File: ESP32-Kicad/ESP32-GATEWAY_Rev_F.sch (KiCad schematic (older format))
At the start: 65 parts, among them J1 Conn_01x07_Male, T1 DTC114YKA, U1 ACPL-217-56AE, U2 TLV62569DBVT(SOT23-5), U3 ESP32-WROOM-32D-4MB, U4 LAN8710A-EZC(QFN32), U5 ACPL-217-56AE

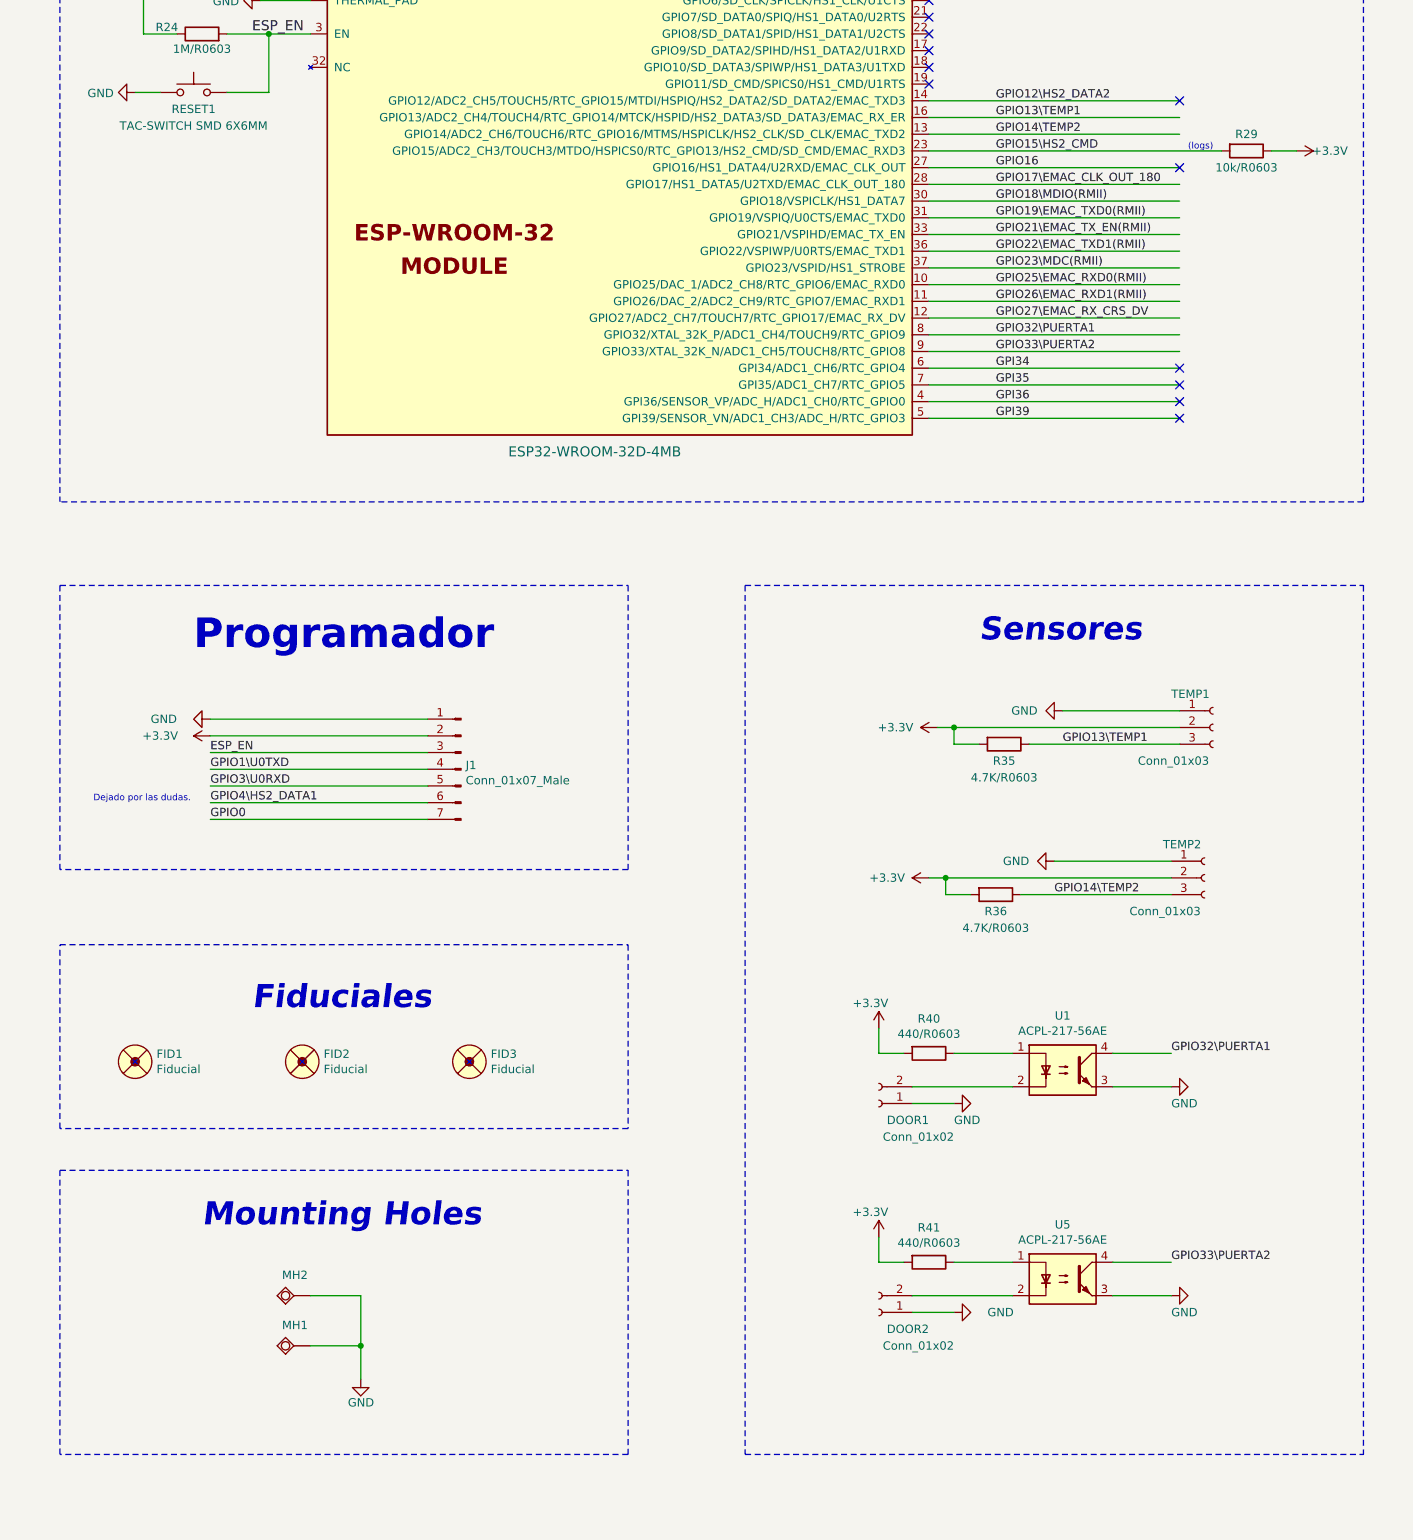
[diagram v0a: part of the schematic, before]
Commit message: Se agregaron 2 sensores de puerta y se sacó uno de temperatura
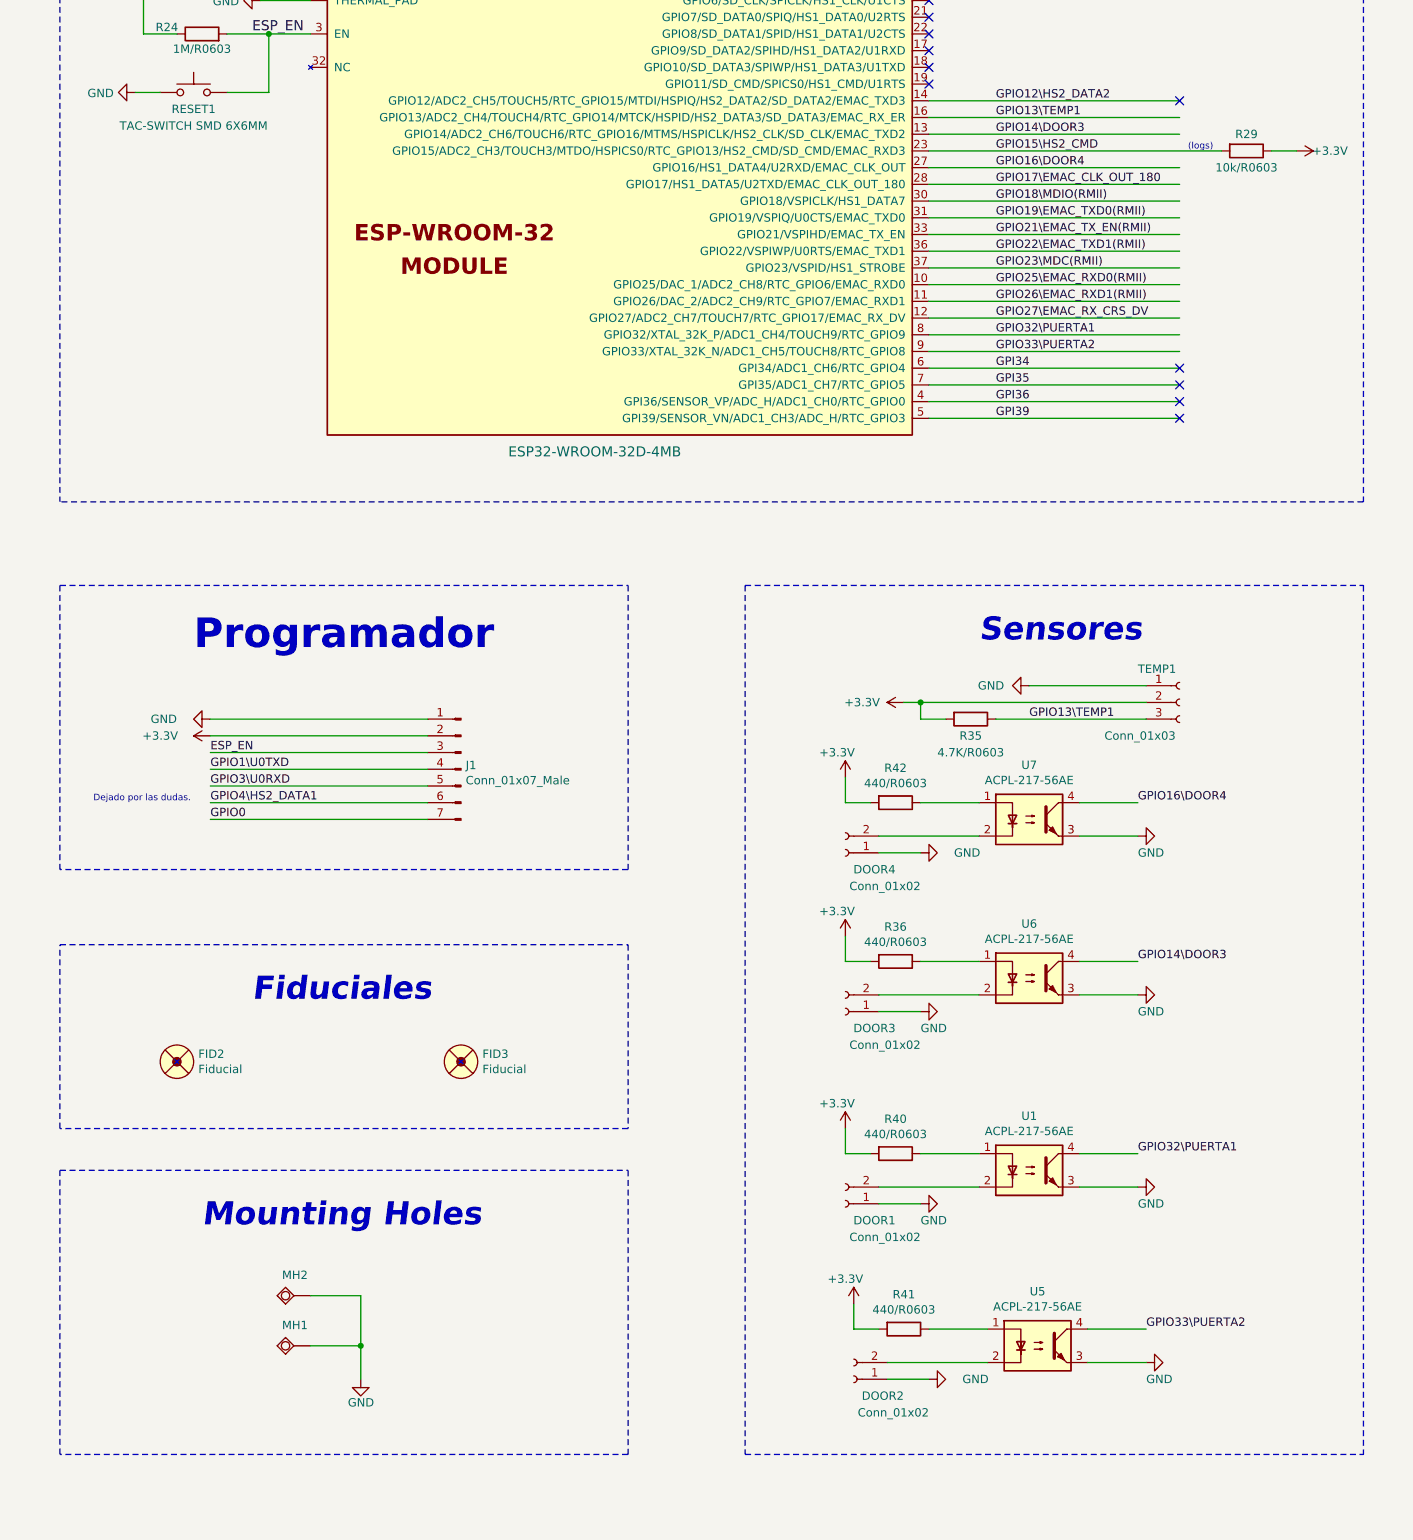
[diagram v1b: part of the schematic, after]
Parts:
- removed FID1: Fiducial, OLIMEX_Other-FP:Fiducial1x3, symbol ESP32-GATEWAY_Rev_F:Fiducial
- removed TEMP2: Conn_01x03, Connector_Molex:Molex_KK-254_AE-6410-03A_1x03_P2.54mm_Vertical, symbol Connector:Conn_01x03_Female
- added DOOR3, DOOR4: Conn_01x02, Connector_Molex:Molex_KK-254_AE-6410-02A_1x02_P2.54mm_Vertical, symbol Connector:Conn_01x02_Female
- added R42: 440/R0603, Resistor_SMD:R_0603_1608Metric_Pad0.98x0.95mm_HandSolder, symbol Device:R
- added U6, U7: ACPL-217-56AE, Package_SO:SO-4_4.4x2.3mm_P1.27mm, symbol Isolator:SFH617A-1
- R36: value 4.7K/R0603 -> 440/R0603
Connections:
- net labels added: GPIO14\DOOR3, GPIO16\DOOR4
- net labels removed: GPIO14\TEMP2, GPIO16
- wire segments 301 -> 309
- no-connect marks 20 -> 19
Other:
- moved on the sheet: DOOR1, DOOR2, FID2, FID3, R35, R40, R41, TEMP1, U1, U5
